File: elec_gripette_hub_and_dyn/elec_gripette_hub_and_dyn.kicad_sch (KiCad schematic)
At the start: 10 parts

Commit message: [update] gripette + bulkhead -B1 in production @JLCPCB
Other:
- note added: "01/06/2026"
- note removed: "ToDo: - DXL/Feetech compat (DIP switch + MOS?) - add jumper for accessing uart-dynamixel from rasp-uart"
- note removed: "dd/mm/2026"

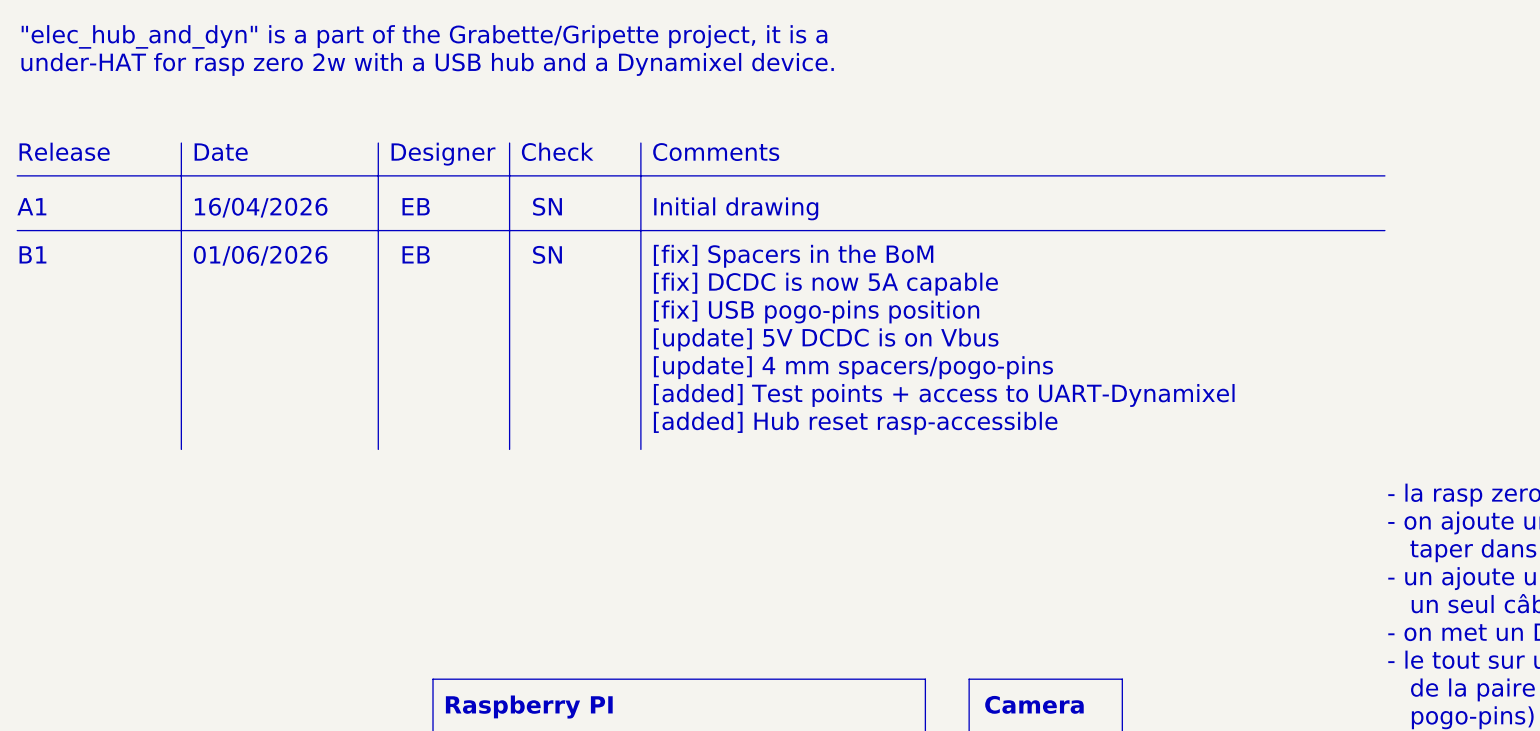
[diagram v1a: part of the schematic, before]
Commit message: [fix] Ajusting cable length
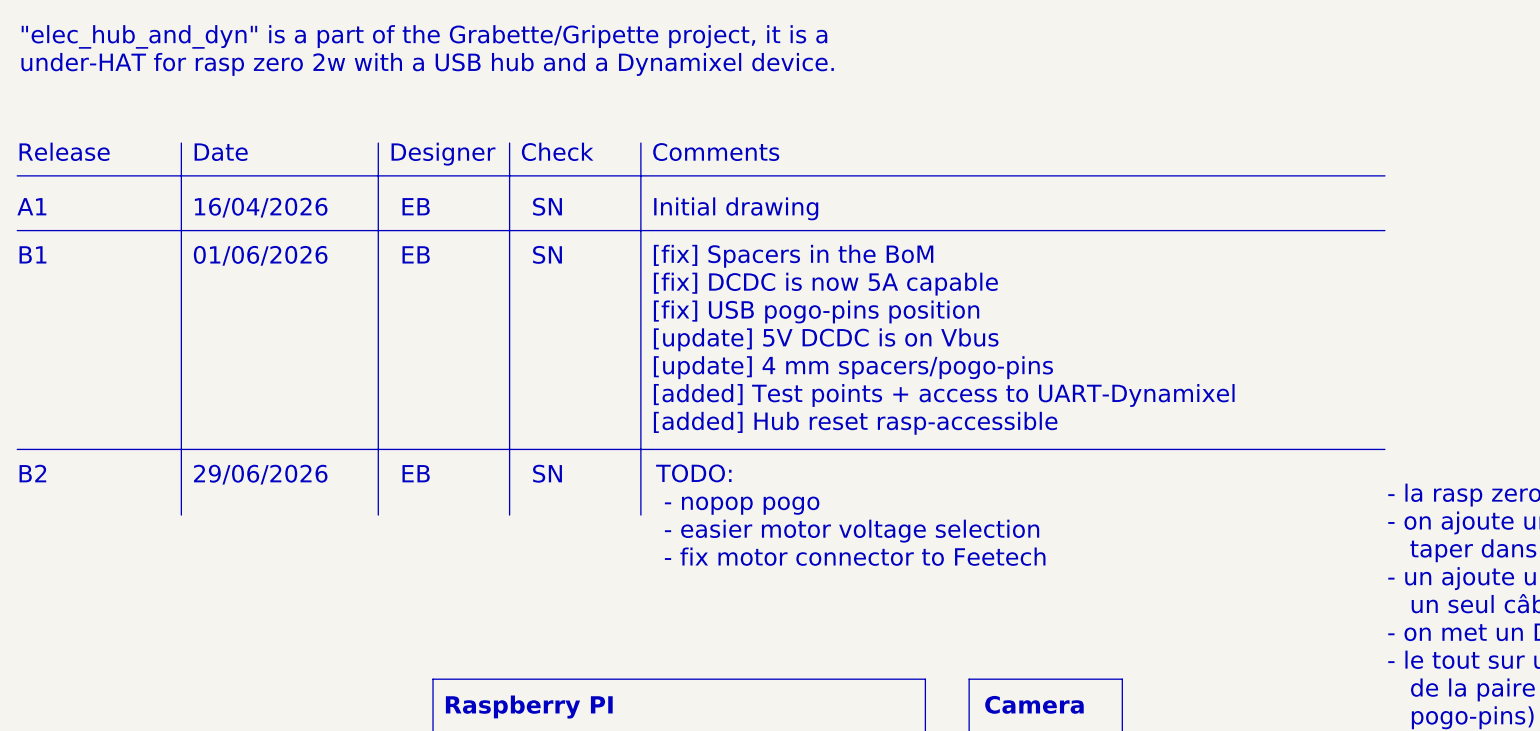
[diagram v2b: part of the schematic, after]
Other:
- note added: "29/06/2026"
- note added: "B2"
- note added: "TODO: - nopop pogo - easier motor voltage selection - fix motor connector to Feetech"
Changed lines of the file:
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@@
+		)
+	)
+	(text "B2"
+		(exclude_from_sim no)
+		(at 19.05 75.438 0)
+		(effects
+			(font
+				(size 2.0066 2.0066)
+			)
+			(justify left bottom)
 		)
 	)
@@
 		)
 	)
+	(text "SN"
+		(exclude_from_sim no)
+		(at 78.74 75.438 0)
+		(effects
+			(font
+				(size 2.0066 2.0066)
+			)
+			(justify left bottom)
+		)
+	)
 	(text "- SO10x: USB connector + Dynamixel/Feetech @7,4V\n- OpenArm: USB connector + 24V on XT60"
 		(exclude_from_sim no)
@@
 		(exclude_from_sim no)
 		(at 62.23 38.1 0)
+		(effects
+			(font
+				(size 2.0066 2.0066)
+			)
+			(justify left bottom)
+		)
+	)
+	(text "TODO: \n - nopop pogo\n - easier motor voltage selection\n - fix motor connector to Feetech"
+		(exclude_from_sim no)
+		(at 93.218 85.09 0)
+		(effects
+			(font
+				(size 2.0066 2.0066)
+			)
+			(justify left bottom)
+		)
+	)
+	(text "EB"
+		(exclude_from_sim no)
+		(at 63.5 75.438 0)
 		(effects
 			(font
@@
 				(bold yes)
 			)
+		)
+	)
+	(text "29/06/2026"
+		(exclude_from_sim no)
+		(at 39.37 75.438 0)
+		(effects
+			(font
+				(size 2.0066 2.0066)
+			)
+			(justify left bottom)
 		)
 	)
@@
 	(polyline
 		(pts
-			(xy 91.44 35.56) (xy 91.44 71.12)
+			(xy 91.44 35.56) (xy 91.44 78.74)
 		)
 		(stroke
@@
 	(polyline
 		(pts
-			(xy 38.1 35.56) (xy 38.1 71.12)
+			(xy 38.1 35.56) (xy 38.1 78.74)
 		)
 		(stroke
@@
 	(polyline
 		(pts
-			(xy 60.96 35.56) (xy 60.96 71.12)
-		)
-		(stroke
-			(width 0)
-			(type default)
-		)
-	)
-	(polyline
-		(pts
-			(xy 76.2 35.56) (xy 76.2 71.12)
+			(xy 60.96 35.56) (xy 60.96 78.74)
+		)
+		(stroke
+			(width 0)
+			(type default)
+		)
+	)
+	(polyline
+		(pts
+			(xy 76.2 35.56) (xy 76.2 78.74)
 		)
 		(stroke
@@
 		)
 		(stroke
+			(width 0)
+			(type default)
+		)
+	)
+	(polyline
+		(pts
+			(xy 19.05 71.12) (xy 177.8 71.12)
+		)
+		(stroke
